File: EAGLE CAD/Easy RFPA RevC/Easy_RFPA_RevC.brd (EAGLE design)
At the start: 152.4 x 165.1 mm, 305 parts, among them IC1 LM741D, IC2 LM741D, IC3 LM393D, IC5 74AHC1G00DBV, IC6 74LS74D, IC7 74AHC1G86DBV, J101 COAX112640BNC_EDGE, J102 COAX112640BNC_EDGE, J301 COAX112640BNC_EDGE, J302 COAX112640BNC_EDGE, J401 HDR_2X1282836-1282836-1, J402 KK_PCFAN, Q1 IRF630, Q101 IRF520N, Q102 IRF630, Q2 MOSFET_NBSS123SOT23, Q201 IRF630, Q202 IRF630, Q3 NPNMMBT3904SOT23_BEC, Q301 MOSFET_NBSS123SOT23, Q302 PNPSOT23_BEC, Q303 NPNMMBT3904SOT23_BEC, Q4 PNPSOT23_BEC, T1 HP1_TRAFO, T102 HP4_TRAFO, U1 OPAMP_QUADTLV274IDSOIC14, U302 OPAMP_QUADTLV274IDSOIC14, U401 LDO_3TERMMC78M12CTGTO220_VERT, U402 LDO_3TERMMC78M05CTGTO220_VERT, X1 1-227161-0, X2 1-227161-0, X3 1-227161-0, X4 1-227161-0, X402 HEATSINK_OMNI_DUALOMNI-UNI-30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

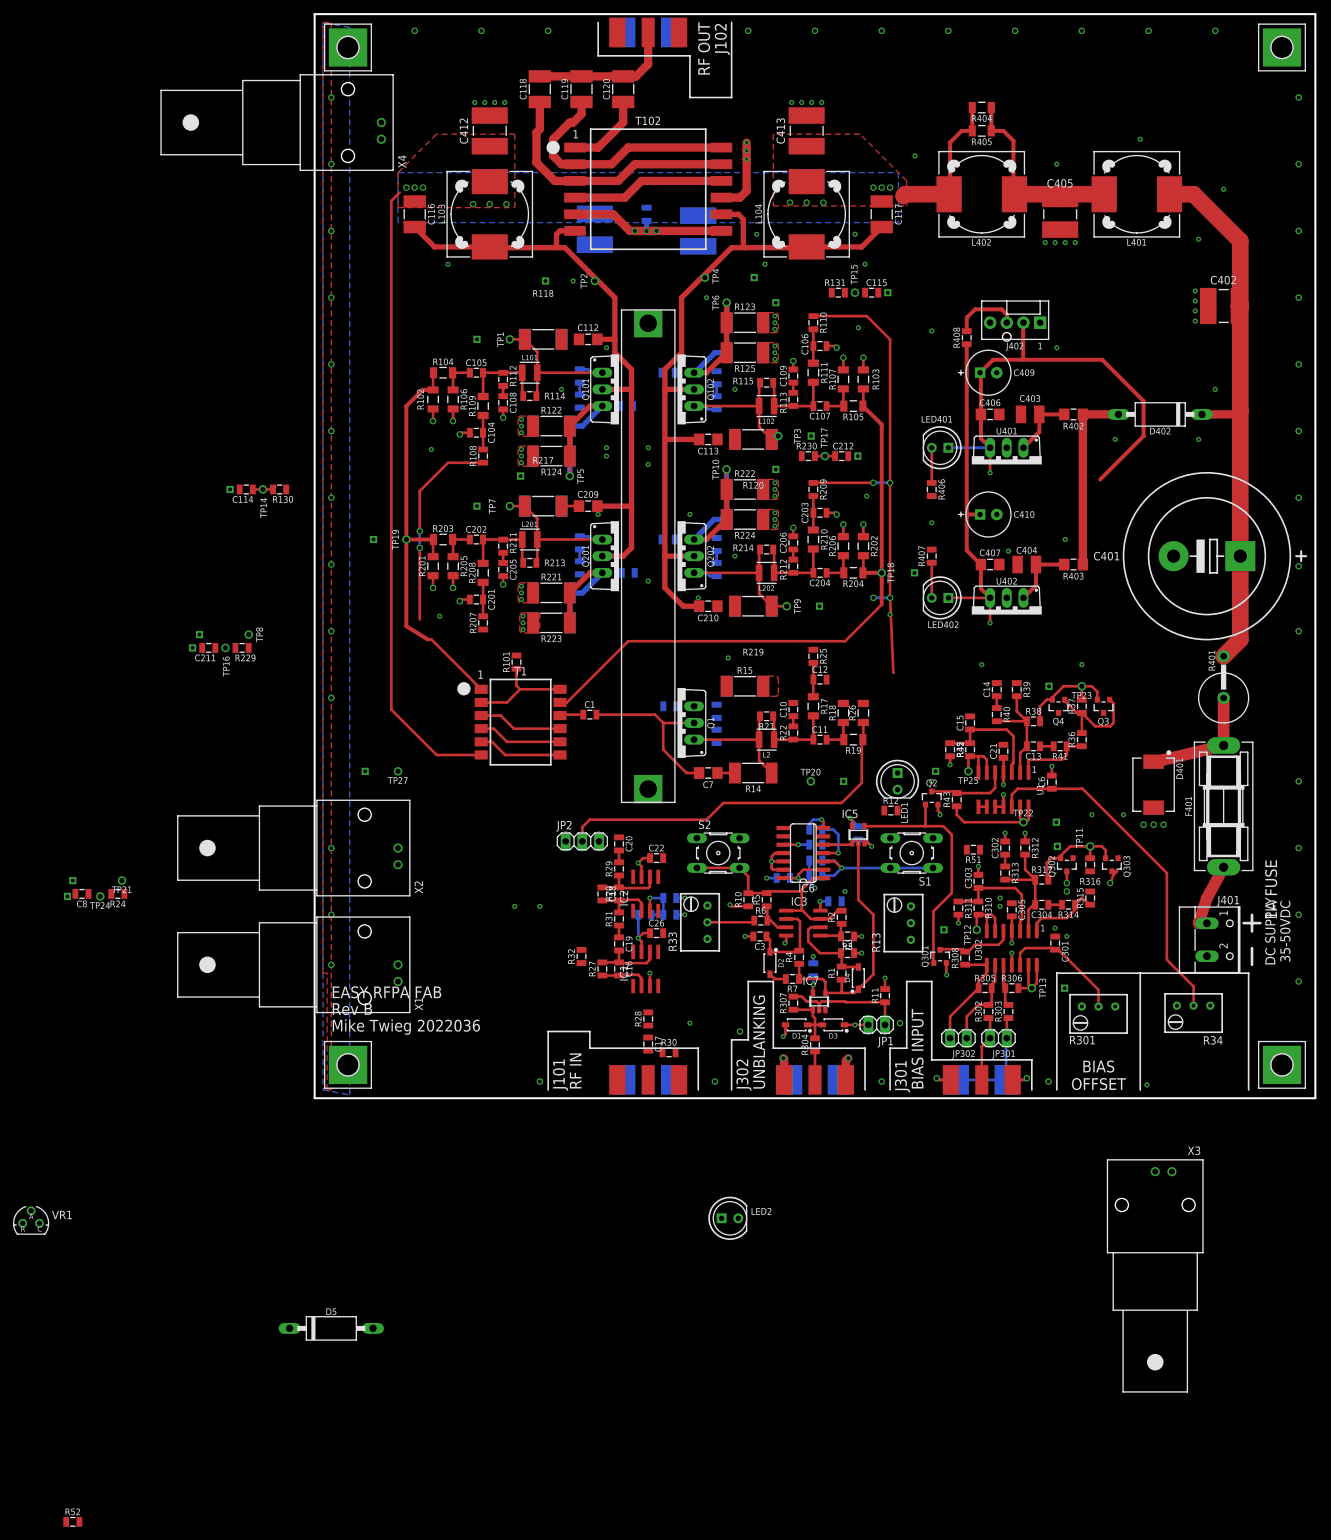
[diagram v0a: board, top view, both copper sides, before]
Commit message: Move connectors/LEDs/buttons to west edge
Aiming to have these poke through a panel.
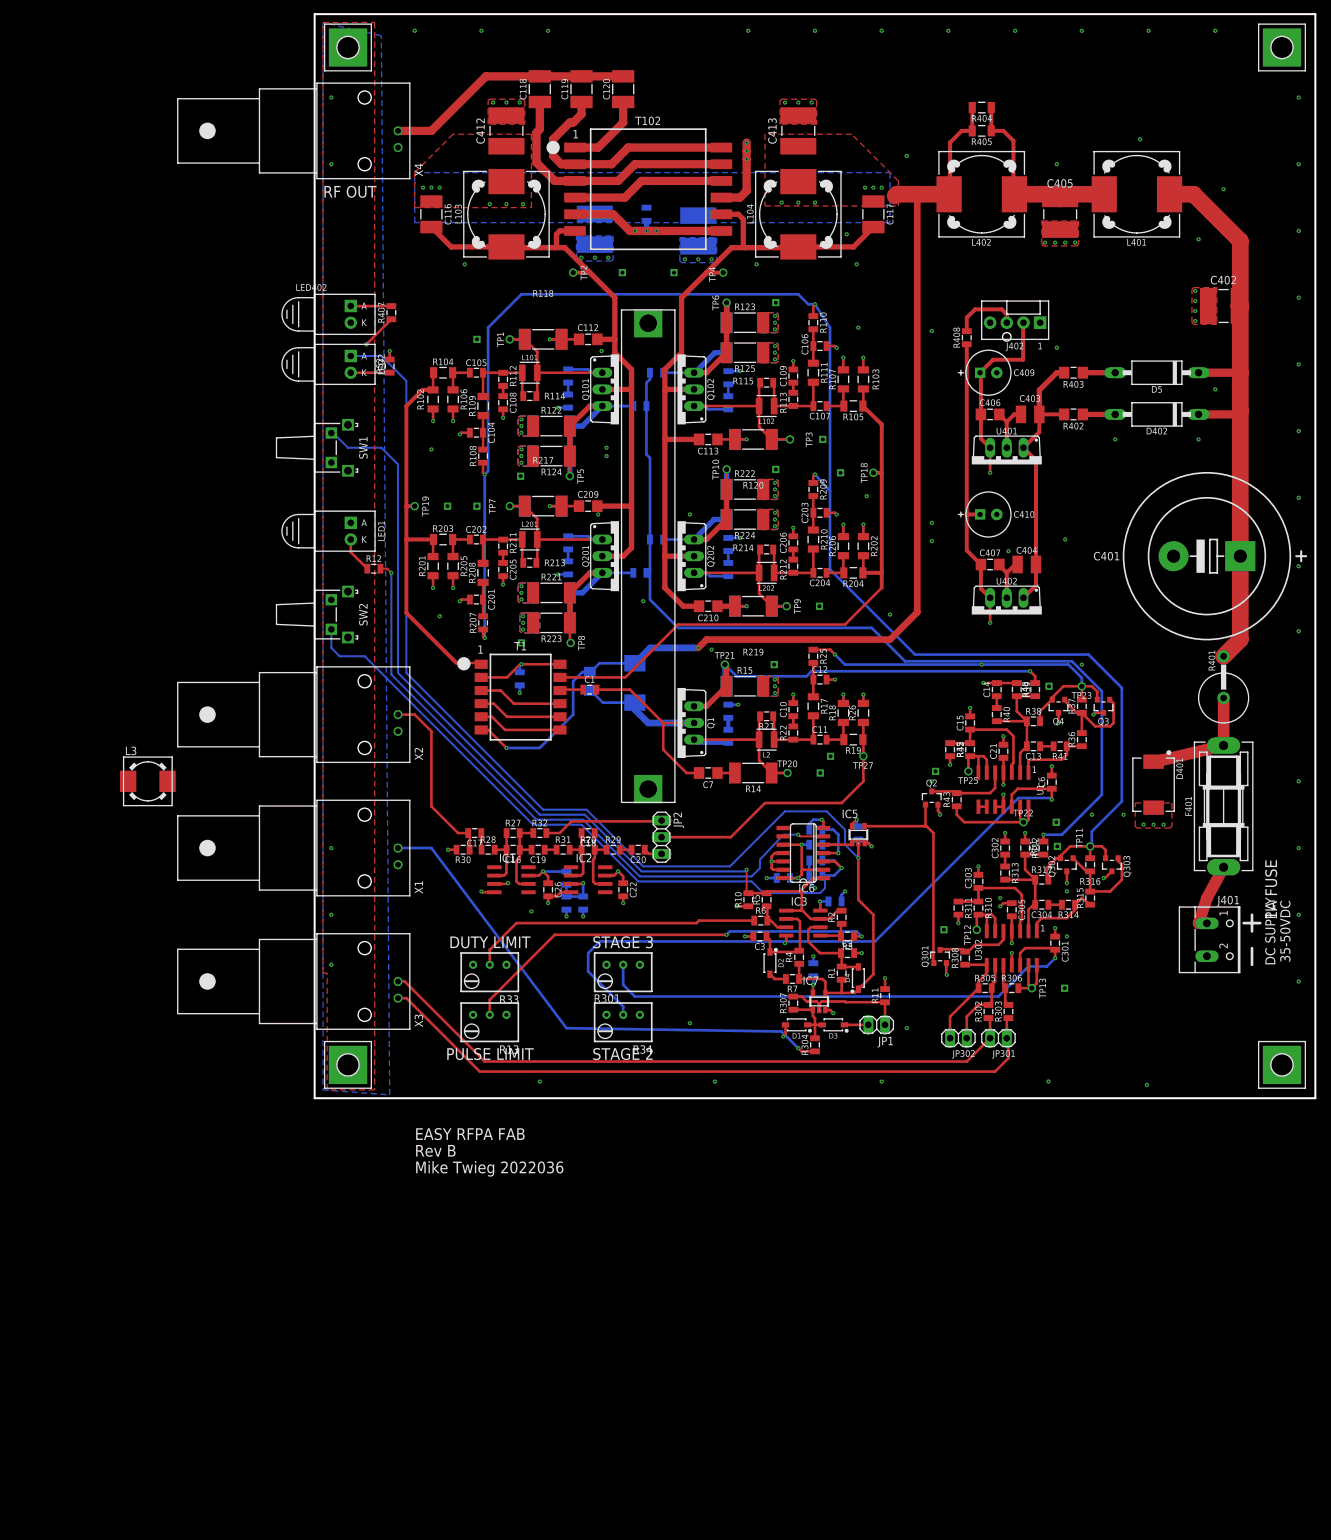
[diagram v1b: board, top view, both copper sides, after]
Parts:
- removed C114, C115, C211, C212: 10nF, MDT_C:0805_IPC-7351B
- removed J101, J102, J301, J302: COAX112640BNC_EDGE, MDT_CON:BNC_EDGE
- removed LED401: LEDHLMP-3962-F0002T1_3/4, MDT_Diode:LED5MM
- removed R130, R131, R229, R230, R24: 1K, MDT_R:0805_IPC-7351B
- removed R406: 2K, MDT_R:0805_IPC-7351B
- removed S1, S2: (no value), switch-omron:B3F-10XX
- removed TP14, TP15, TP16, TP17, TP24: PROBE_TPTP_5MM, MDT_CON:PROBE_TP_5MM
- removed VR1: (no value), v-reg:TO92-CLP
- added L1: (no value), MDT_L:DR74
- added L3: DR74, inductors:DR74
- added SW1, SW2: SPST_NO_TACT_RA431256083716431256083716, MDT_SWITCH:431256083716
- C8: value 10nF -> 22nF; device MDT_C:0805_IPC-7351B -> MDT_C:C1206
- LED1, LED2: value LEDHLMP-3401-E0002T1_3/4 -> LEDT1_3/4_RA; device MDT_Diode:LED5MM -> MDT_Diode:LED_5MM_RA
- LED402: value LEDHLMP-3962-F0002T1_3/4 -> LEDT1_3/4_RA; device MDT_Diode:LED5MM -> MDT_Diode:LED_5MM_RA
- moved D5 192.3 mm to (128.3, 97.8), turned to 180 degrees
- moved R52 182.5 mm to (11.4, 98.8), turned to 90 degrees
- moved LED2 144.6 mm to (0.00, 99.1)
- moved X3 125.1 mm to (7.62, 5.08), turned to 90 degrees
- moved LED402 104.6 mm to (0.00, 106.7), turned to 0 degrees
- moved TP21 97.5 mm to (62.5, 53.3), turned to 0 degrees
- moved LED1 96.6 mm to (0.00, 73.7), turned to 0 degrees
- moved R407 90.3 mm to (11.7, 106.9)
- moved R12 86.9 mm to (9.02, 67.9)
- moved R34 86.9 mm to (47.0, -1.27)
- moved C8 83.8 mm to (41.9, 50.8), flipped to the bottom, turned to 270 degrees
- moved R301 72.7 mm to (47.0, 6.35)
- moved TP27 70.9 mm to (83.6, 39.4)
- moved R13 64.7 mm to (26.7, -1.27), turned to 90 degrees
- moved R48 55.7 mm to (109.7, 49.5), flipped to the top, turned to 90 degrees
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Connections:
- removed net AN6: C115.1, R131.2, TP15.TP
- removed net AP6: C114.1, R130.2, TP14.TP
- removed net BN6: C212.1, R230.2, TP17.TP
- removed net BP6: C211.1, R229.2, TP16.TP
- removed net N$49: C404.1, R403.2, U402.1
- removed net S1_BP6: C8.1, R24.2, TP24.TP
- net !FAULT: now also SW1.2; no longer S2.3, S2.4
- net +12V: no longer LED401.A
- net +5V: now also R407.1, SW2.2; no longer LED402.A, S1.3, S1.4
- net AN5: no longer R131.1
- net AP5: no longer R130.1
- net BN5: no longer R230.1
- net BP5: no longer R229.1
- net GND: now also LED402.K, SW1.1, SW1.3, SW1.4, SW2.1, SW2.4; no longer C114.2, C115.2, C211.2, C212.2, C8.2, J101.G1, J101.G2, J101.G3, J101.G4, J102.G1, J102.G2, J102.G3, J102.G4, J302.G1, J302.G2, J302.G3, J302.G4, R406.2, R407.2, S2.1, S2.2, TP14.GND, TP15.GND, TP16.GND, TP17.GND, TP24.GND
- net N$20: no longer J301.C
- net N$21: no longer J301.G1, J301.G2, J301.G3, J301.G4
- net N$28: now also D5.A; no longer D402.A, R402.1
- net N$31: no longer J102.C
- net N$32: now also D402.A, R402.1; no longer LED401.K, R406.1
- net N$33: now also LED402.A, R407.2; no longer LED402.K, R407.1
- net N$43: now also C404.1, R403.2, U402.1
- net N$46: now also D5.C
- net N$53: no longer J302.C
- net N$69: no longer J101.C
- net RESET: now also SW2.3; no longer S1.1, S1.2
- net S1_BP5: no longer R24.1
- net S2_DP: now also C8.2, L1.1
- net VB: now also C8.1, L1.2
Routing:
- net N$77: track 39.6 -> 182.9 mm, vias 0 -> 1
- net N$22: track 0.00 -> 138.6 mm, vias 0 -> 1
- net S3_GBIAS: track 125.5 -> 244.9 mm, vias 6 -> 4
- net !FAULT: track 36.1 -> 138.5 mm, vias 0 -> 1
- net !READY: track 0.00 -> 99.5 mm, vias 0 -> 2
- net N$20: track 10.0 -> 99.9 mm
- net RESET: track 24.0 -> 105.9 mm
- net N$21: track 28.0 -> 104.9 mm, vias 2 -> 0
- net N$53: track 4.34 -> 78.5 mm, vias 0 -> 1
- net N$59: track 1.16 -> 64.7 mm, vias 1 -> 2
- net S1_BP5: track 0.00 -> 62.7 mm, vias 0 -> 1
- net N$25: track 19.3 -> 81.4 mm, vias 0 -> 1
- net GND: track 95.6 -> 144.8 mm, vias 183 -> 190
- net N$64: track 53.0 -> 102.1 mm, vias 0 -> 1
- net VB: track 118.5 -> 166.7 mm, vias 12 -> 14
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- added copper zone on layer 15, net +12V
- added copper zone on layer 15, net +24V
- added copper zone on layer 15, net +5V
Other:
- board text added: "DUTY LIMIT"
- board text added: "PULSE LIMIT"
- board text added: "STAGE 2"
- board text added: "STAGE 3"
- board text removed: "BIAS INPUT"
- board text removed: "BIAS OFFSET"
- board text removed: "RF IN"
- board text removed: "UNBLANKING"

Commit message: Try and keep area under 30 square inches
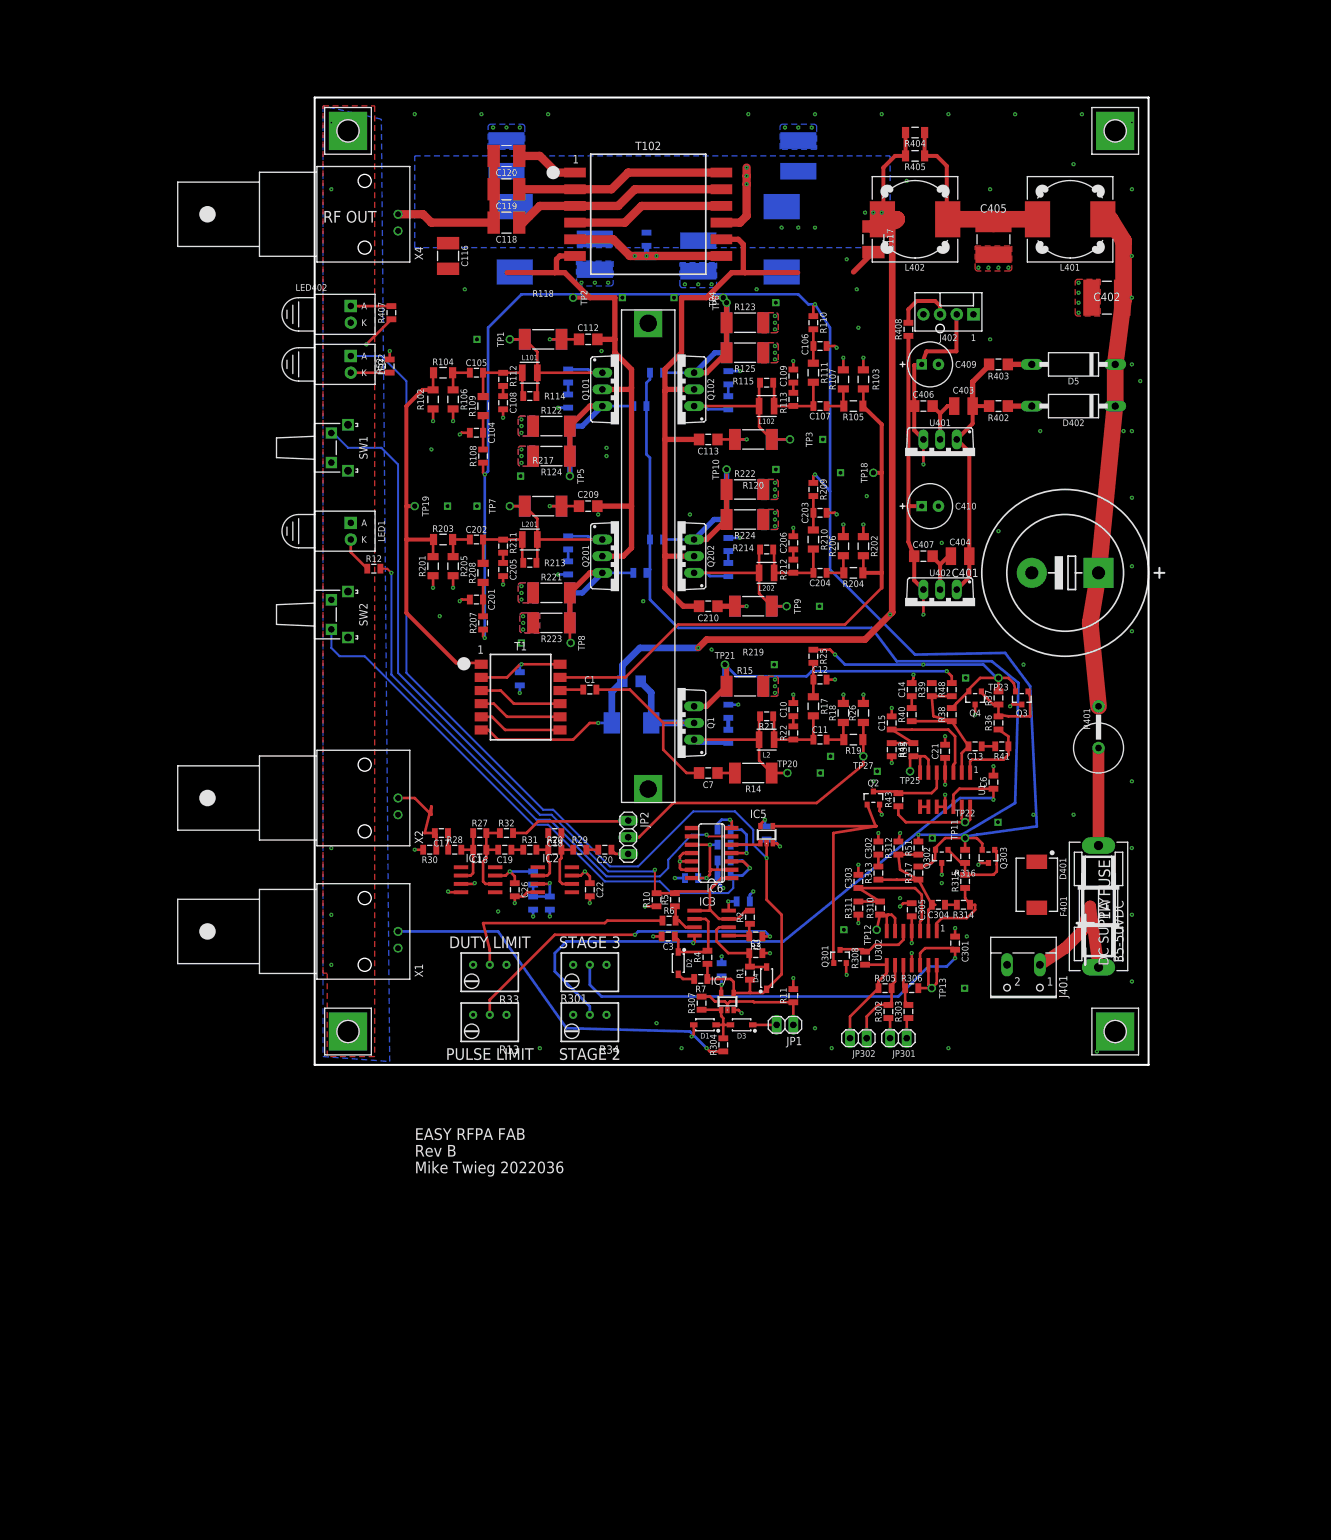
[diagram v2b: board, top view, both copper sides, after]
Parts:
- removed L3: DR74, inductors:DR74
- removed X3: 1-227161-0, con-coax:AMP_227161
- moved J401 29.6 mm to (108.0, 6.35), turned to 180 degrees
- moved H403 28.4 mm to (121.9, 134.6)
- moved H402 25.9 mm to (121.9, -2.54)
- moved F401 24.4 mm to (119.4, 16.5)
- moved D401 23.4 mm to (110.0, 19.8)
- moved C401 21.7 mm to (114.3, 67.3)
- moved C118 20.9 mm to (29.2, 120.7), turned to 180 degrees
- moved R401 20.5 mm to (119.4, 45.7)
- moved C120 20.5 mm to (29.2, 130.8), turned to 180 degrees
- moved C302 19.3 mm to (85.9, 25.4)
- moved R313 19.3 mm to (85.9, 21.6)
- moved R312 19.3 mm to (88.9, 25.4)
- moved R315 19.2 mm to (99.1, 20.3)
- moved Q302 19.1 mm to (95.5, 24.1)
- moved R316 19.1 mm to (99.1, 24.1)
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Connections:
- net N$20: no longer X3.1
- net N$21: no longer X3.2
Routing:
- net N$21: track 104.9 -> 3.32 mm
- net N$20: track 99.9 -> 3.17 mm
- net N$53: track 78.5 -> 58.4 mm
- net S2_GBIAS: track 59.6 -> 45.2 mm
- net DRAINS_POS: track 96.7 -> 82.3 mm
- net RESET: track 105.9 -> 91.9 mm
- net !READY: track 99.5 -> 85.6 mm
- net N$59: track 64.7 -> 50.7 mm
- net N$77: track 182.9 -> 168.9 mm
- net !FAULT: track 138.5 -> 124.5 mm
- net +5V: track 226.9 -> 213.4 mm
- net VB: track 166.7 -> 153.5 mm, vias 14 -> 8
- net N$46: track 91.1 -> 78.1 mm
- net S1_BP5: track 62.7 -> 50.0 mm
- net N$31: track 37.7 -> 25.2 mm
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- removed copper zone on layer 1, net VB
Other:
- board size 152.4 x 165.1 mm -> 127 x 147.3 mm
